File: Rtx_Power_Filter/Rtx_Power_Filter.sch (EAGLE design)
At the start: 22 parts

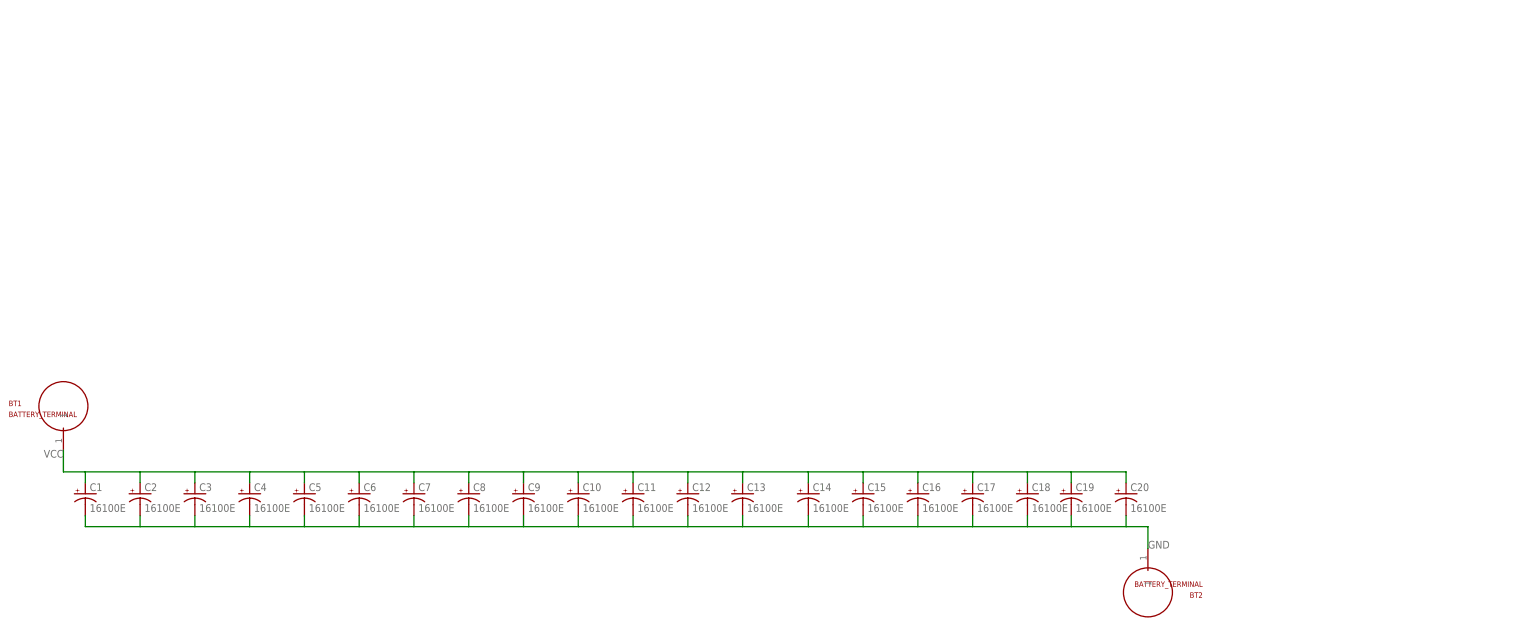
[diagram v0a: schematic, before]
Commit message: Completed RTx Power Filter Board.
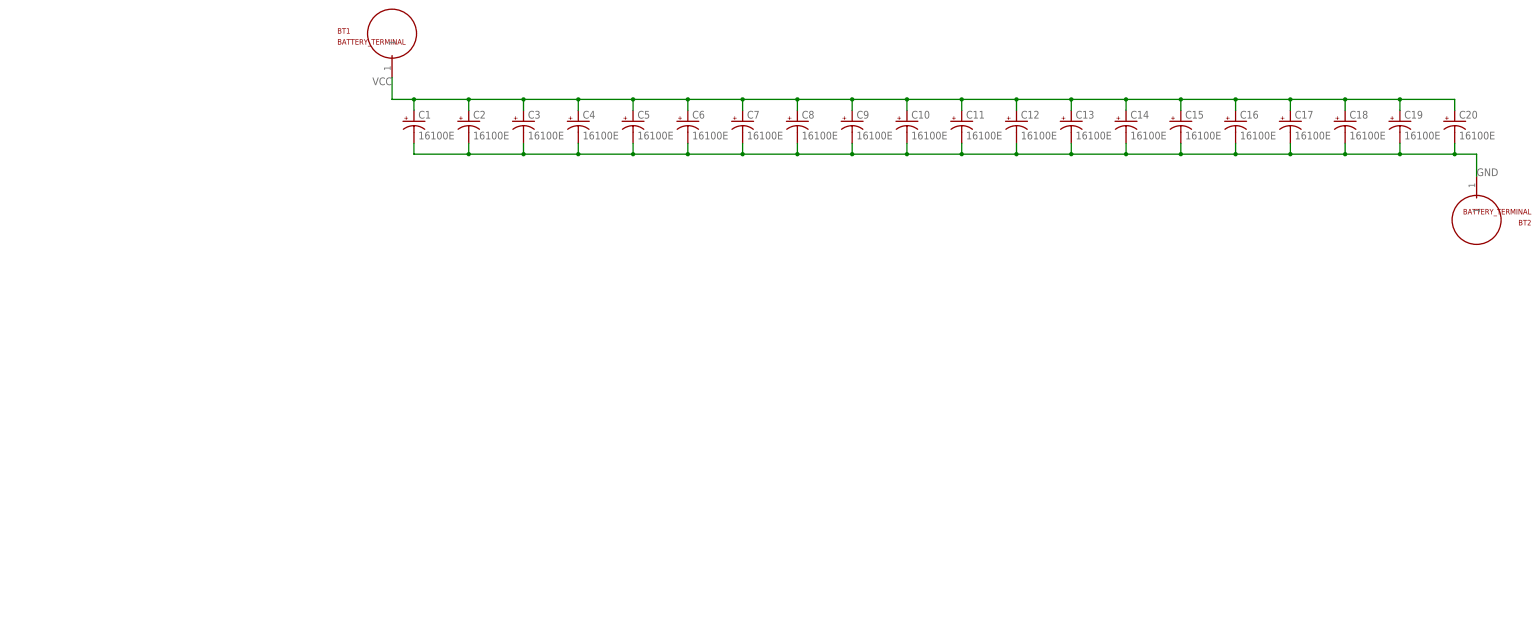
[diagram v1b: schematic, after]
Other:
- moved on the sheet: BT1, BT2, C1, C10, C11, C12, C13, C14, C15, C16, C17, C18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
